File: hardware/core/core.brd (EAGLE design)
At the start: 131.8 x 142.2 mm, 280 parts, among them IC1 MAX481CSA, IC10 MAX481CSA, IC11 MAX481CSA, IC12 MAX481CSA, IC13 MAX481CSA, IC14 MAX481CSA, IC15 MAX481CSA, IC16 MAX481CSA, IC17 MAX481CSA, IC18 MAX481CSA, IC19 MAX481CSA, IC2 LD117AS12TR, IC20 MAX481CSA, IC21 MAX481CSA, IC3 MAX481CSA, IC4 MAX481CSA, IC5 MAX481CSA, IC6 MAX481CSA, IC7 MAX481CSA, IC8 MAX481CSA, IC9 MAX481CSA

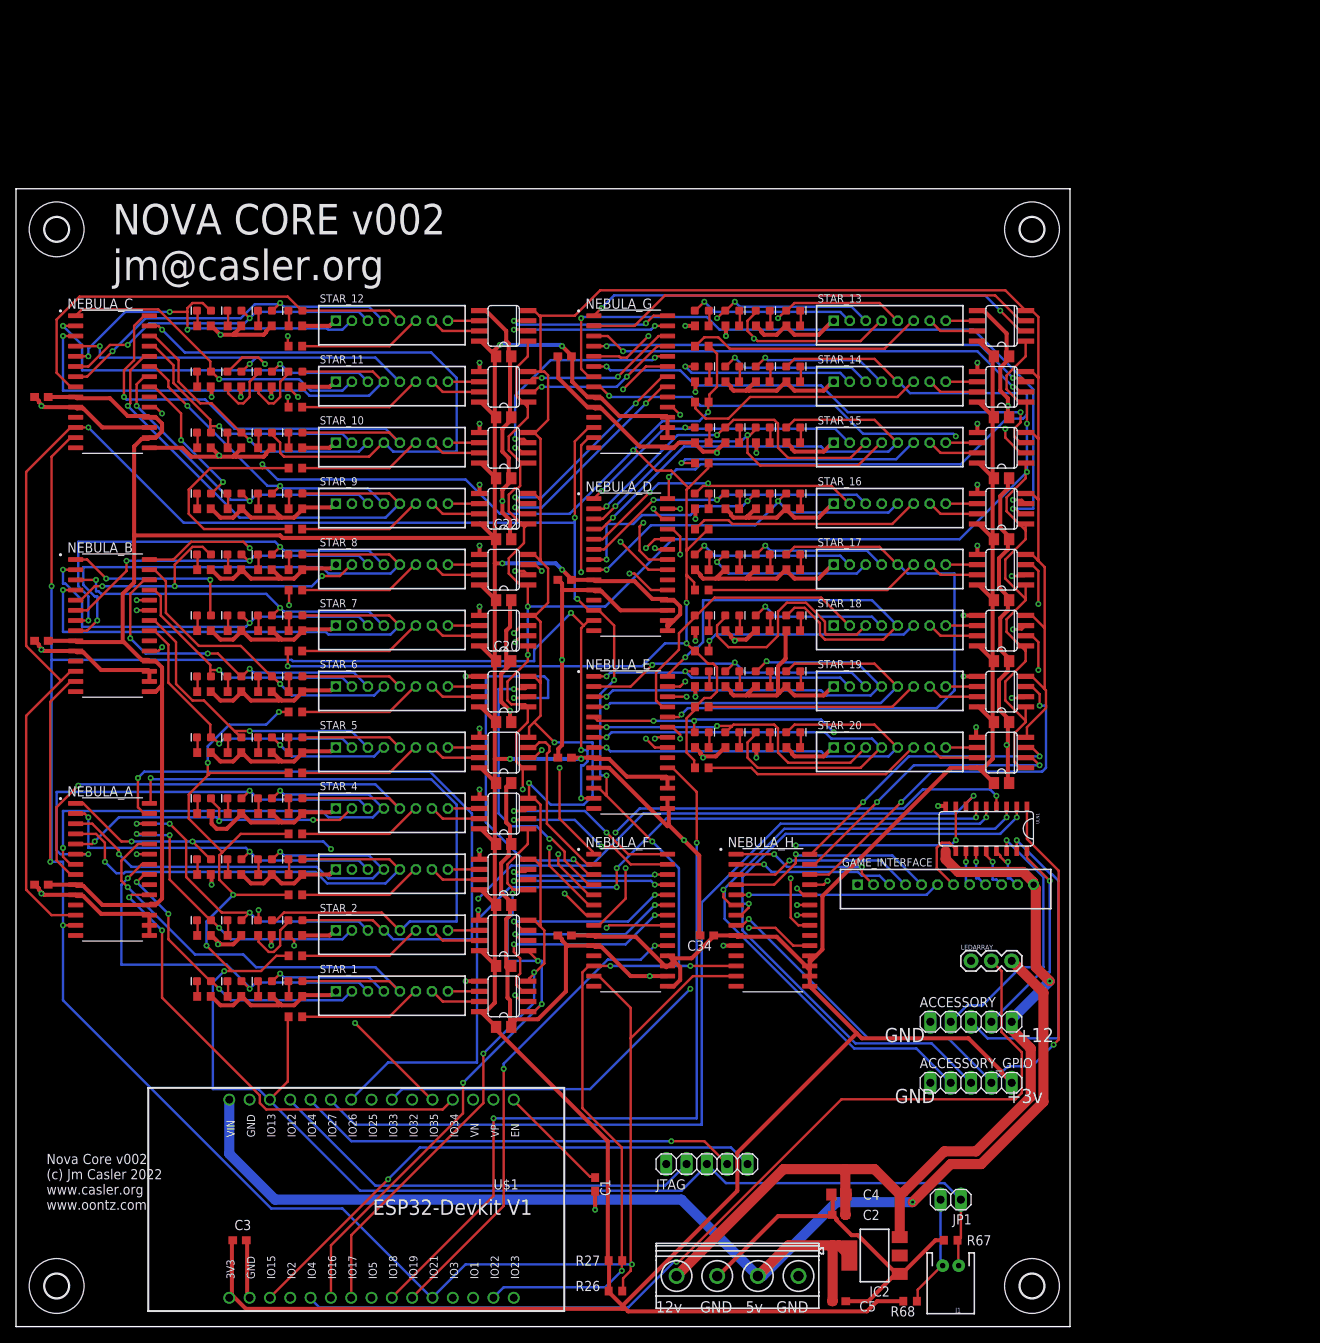
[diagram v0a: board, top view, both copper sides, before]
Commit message: Nova 3.0 in progress. Needs line drivers.
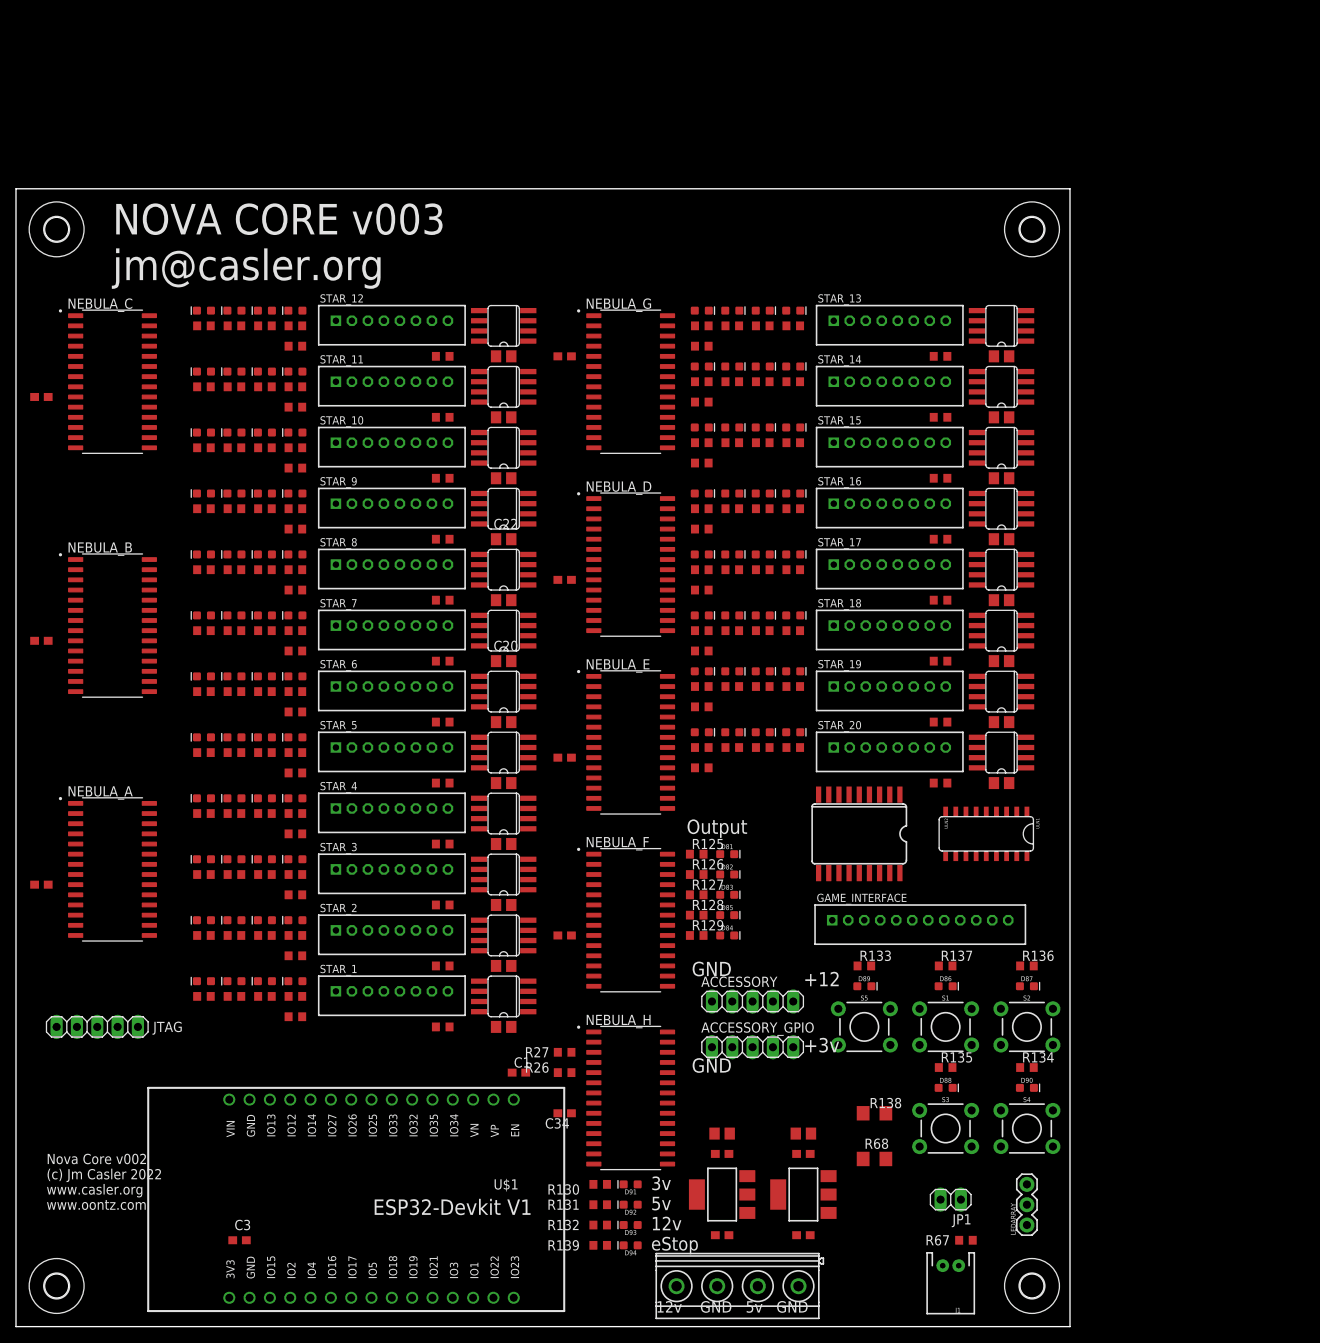
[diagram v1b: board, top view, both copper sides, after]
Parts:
- added C35, C36: 10uf, rcl:C0603
- added C6: 1uf, rcl:C0805
- added D81, D86, D91: red, SparkFun-LED:LED-0603
- added D82, D87, D92: green, SparkFun-LED:LED-0603
- added D83, D88, D93: blue, SparkFun-LED:LED-0603
- added D84, D89: white, SparkFun-LED:LED-0603
- added D85, D90, D94: yellow, SparkFun-LED:LED-0603
- added IC22: LD117AS12TR, v-reg:SOT223
- added R1, R107, R108, R109, R110, R111, R112, R113, R114, R115, R116, R117, R118, R119, R120, R121, R122, R123, R124, R2: 120, rcl:R0603
- added R125, R126, R127, R128, R129, R130, R139: 1k, rcl:R0603
- added R131: 2.2k, rcl:R0603
- added R132: 12k, rcl:R0603
- added R133, R134, R135, R136, R137: 10k, rcl:R0603
- added R138: 10, rcl:R1206
- added S1, S2, S3, S4, S5: MOMENTARY-SWITCH-SPST-PTH-6.0MM, SparkFun-Switches:TACTILE_SWITCH_PTH_6.0MM
- added ULN2: (no value), SparkFun-IC-Special-Function:SO18L
- R68: value 68 -> 10; device rcl:R0603 -> rcl:R1206
- moved JTAG 78.1 mm to (10.2, 37.5)
- moved LEDARRAY 33.8 mm to (126.4, 12.7), turned to 90 degrees
- moved C34 28.5 mm to (68.6, 26.7)
- moved NEBULA_H 28.5 mm to (76.8, 28.6)
- moved R26 28.0 mm to (68.6, 31.8)
- moved ACCESSORY_GPIO 27.7 mm to (92.1, 34.9)
- moved ACCESSORY 27.4 mm to (92.1, 40.6)
- moved R27 26.8 mm to (68.6, 34.3)
- moved IC2 20.5 mm to (88.3, 16.5)
- moved R68 18.3 mm to (107.3, 21.0), turned to 0 degrees
- moved C1 16.9 mm to (62.9, 31.8), turned to 0 degrees
- moved C5 16.8 mm to (88.3, 11.4)
- moved C2 16.5 mm to (88.3, 21.6)
- moved C4 16.5 mm to (88.3, 24.1)
- moved GAME_INTERFACE 5.46 mm to (113.0, 50.8)
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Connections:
- new net N$151: D84.A, R129.2
- new net N$152: D85.A, R128.2
- new net N$153: D83.A, R127.2
- new net N$154: D82.A, R126.2
- new net N$155: D81.A, R125.2
- new net N$156: D91.C, R130.1
- new net N$157: D92.C, R131.1
- new net N$158: D93.C, R132.1
- new net N$159: D94.C, R139.1
- net +12V: now also D93.A, ULN2.10
- net +3V3: now also C36.1, D86.A, D87.A, D88.A, D89.A, D90.A, D91.A, IC22.4, R133.1, R134.1, R135.1, R136.1, R137.1, R138.2
- net +5V: now also C35.1, C6.1, D92.A, IC22.3, R125.1, R126.1, R127.1, R128.1, R129.1
- net 13: now also D94.A
- net 23: now also ULN2.8
- net 25: now also ULN2.7
- net 26: now also ULN2.6
- net 27: now also ULN2.5
- net 32: now also ULN2.4
- net GND: now also C35.2, C36.2, C6.2, IC22.1, R130.2, R131.2, R132.2, R139.2, S1.3, S2.3, S3.3, S4.3, S5.3, ULN2.9
- net H10: now also D88.C, R135.2, S3.1
- net H11: now also D90.C, R134.2, S4.1
- net H12: now also D89.C, R133.2, S5.1
- net H13: now also ULN2.3
- net H14: now also ULN2.2
- net H15: now also ULN2.1
- net H8: now also D86.C, R137.2, S1.1
- net H9: now also D87.C, R136.2, S2.1
- net N$108: now also R1.2
- net N$109: now also R1.1
- net N$110: now also R2.2
- net N$111: now also R2.1
- net N$112: now also R107.2
- net N$113: now also R107.1
- net N$114: now also R108.2
- net N$115: now also R108.1
- net N$116: now also R109.2
- net N$117: now also R109.1
- net N$118: now also R110.2
- net N$119: now also R110.1
- net N$120: now also R111.2
- net N$121: now also R111.1
- net N$122: now also R112.2
- net N$123: now also R112.1
- net N$124: now also R113.2
- net N$125: now also R113.1
- net N$126: now also R114.2
- net N$127: now also R114.1
- net N$128: now also R115.2
- net N$129: now also R115.1
- net N$130: now also R116.2
- net N$131: now also R116.1
- net N$132: now also R117.2
- net N$133: now also R117.1
- net N$134: now also R118.2
- net N$135: now also R118.1
- net N$136: now also R119.2
- net N$137: now also R119.1
- net N$138: now also R120.2
- net N$139: now also R120.1
- net N$140: now also R121.2
- net N$141: now also R121.1
- net N$142: now also R122.2
- net N$143: now also R122.1
- net N$144: now also R123.2
- net N$145: now also R123.1
- net N$146: now also R124.2
- net N$147: now also R124.1
- net N$148: now also ULN2.16
- net N$149: now also ULN2.17
- net N$150: now also ULN2.18
- net N$51: now also D81.C, ULN2.11
- net N$56: now also D82.C, ULN2.12
- net N$57: now also D83.C, ULN2.13
- net N$58: now also D85.C, ULN2.14
- net N$59: now also D84.C, ULN2.15
- net N$89: now also R138.1
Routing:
- net GND: track 750.6 -> 0.00 mm, vias 50 -> 0
- net +3V3: track 726.2 -> 0.00 mm, vias 6 -> 0
- net 13: track 470.0 -> 0.00 mm, vias 14 -> 0
- net 21/SDA: track 366.5 -> 0.00 mm, vias 8 -> 0
- net 16: track 309.2 -> 0.00 mm, vias 9 -> 0
- net 17: track 305.9 -> 0.00 mm, vias 4 -> 0
- net 22/SCL: track 296.7 -> 0.00 mm, vias 9 -> 0
- net +5V: track 163.7 -> 0.00 mm, vias 1 -> 0
- net 33: track 137.3 -> 0.00 mm, vias 3 -> 0
- net 36: track 120.4 -> 0.00 mm, vias 1 -> 0
- net 4: track 118.7 -> 0.00 mm, vias 1 -> 0
- net 27: track 116.8 -> 0.00 mm, vias 1 -> 0
- net +12V: track 111.2 -> 0.00 mm, vias 1 -> 0
- net 26: track 105.9 -> 0.00 mm, vias 3 -> 0
- net 25: track 99.6 -> 0.00 mm, vias 2 -> 0
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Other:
- board text added: "3v 5v 12v eStop"
- board text added: "NOVA CORE v003 jm@casler.org"
- board text added: "Output"
- board text removed: "NOVA CORE v002 jm@casler.org"

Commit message: start of adding ULN to the outputs
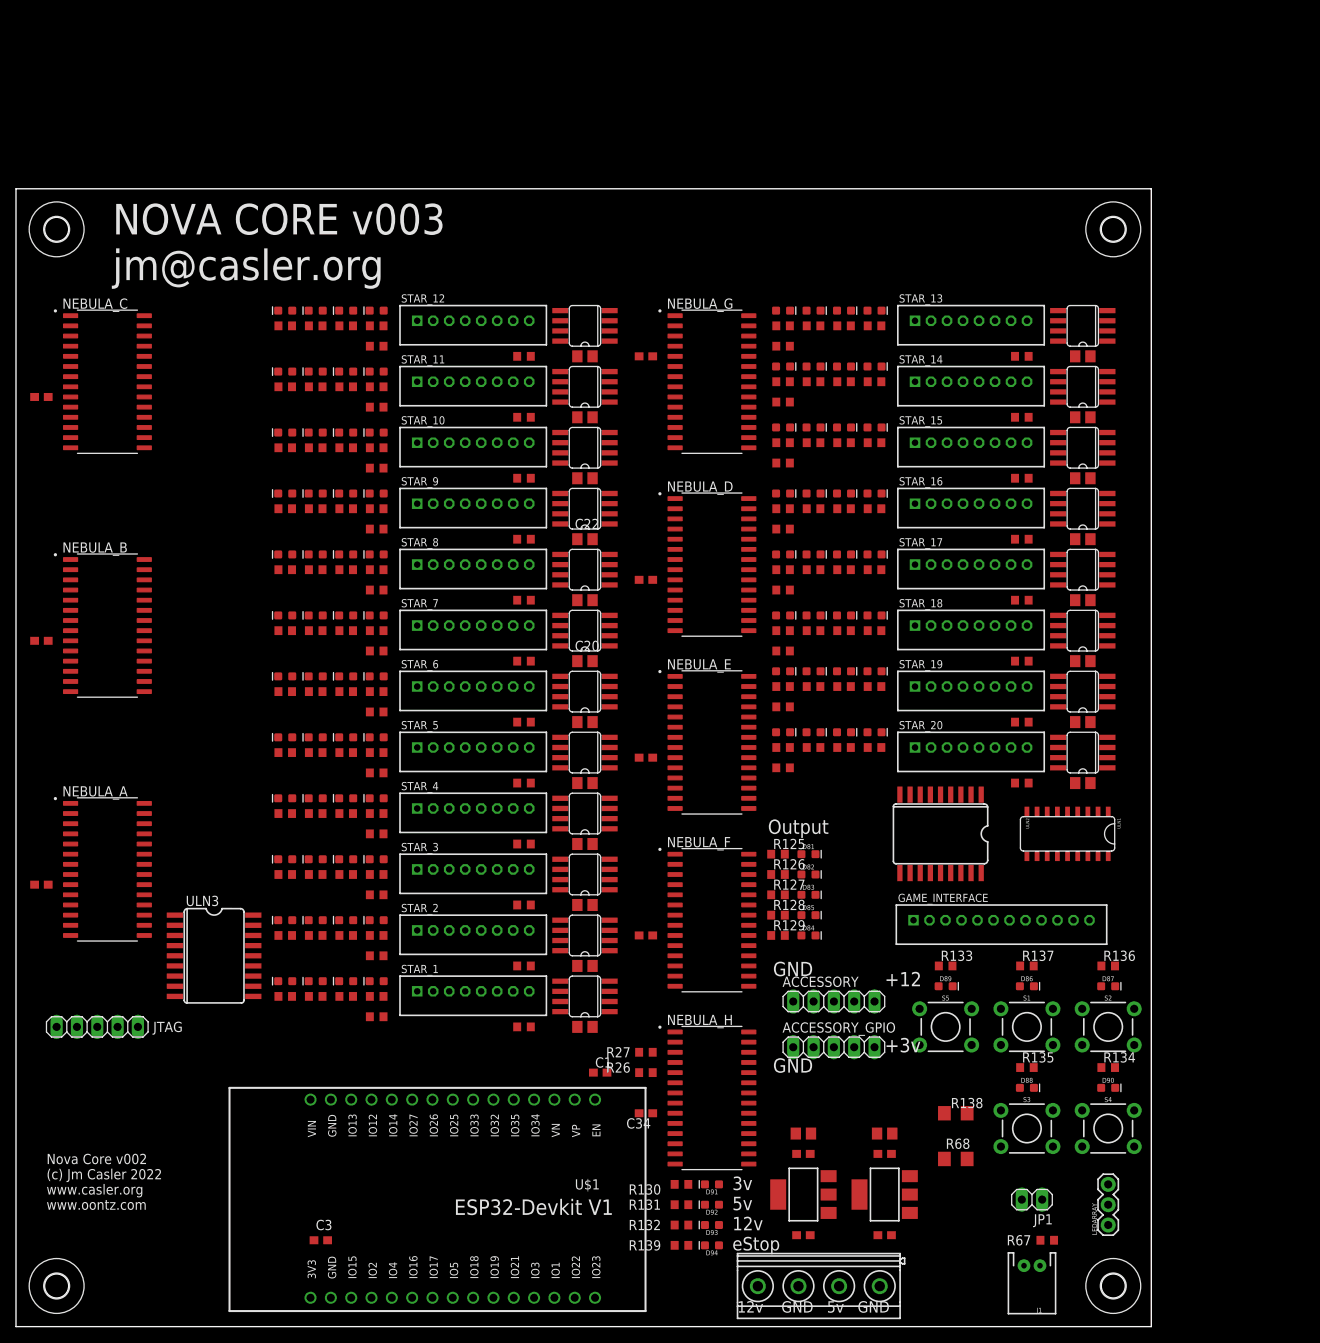
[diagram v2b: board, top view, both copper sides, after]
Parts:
- added ULN3: (no value), SparkFun-IC-Special-Function:SO18L
- moved D1 10.2 mm to (95.9, 127.0)
- moved D53 10.2 mm to (95.9, 120.0)
- moved D57 10.2 mm to (95.9, 112.4)
- moved D61 10.2 mm to (95.9, 104.1)
- moved D65 10.2 mm to (95.9, 96.5)
- moved D69 10.2 mm to (95.9, 88.9)
- moved D73 10.2 mm to (95.9, 81.9)
- moved D77 10.2 mm to (95.9, 74.3)
- moved D87 10.2 mm to (136.5, 42.5)
- moved D90 10.2 mm to (136.5, 29.8)
- moved D91 10.2 mm to (87.0, 17.8)
- moved D92 10.2 mm to (87.0, 15.2)
- moved D93 10.2 mm to (87.0, 12.7)
- moved D94 10.2 mm to (87.0, 10.2)
- moved LEDARRAY 10.2 mm to (136.5, 12.7)
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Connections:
- new net N$160: R3.1, STAR_1.2, ULN3.11
- new net N$161: R4.1, STAR_1.3, ULN3.12
- new net N$162: R5.1, STAR_1.4, ULN3.13
- new net N$163: R6.1, STAR_1.5, ULN3.14
- new net N$164: R10.1, STAR_2.5, ULN3.18
- new net N$165: R9.1, STAR_2.4, ULN3.17
- new net N$166: R8.1, STAR_2.3, ULN3.16
- new net N$167: R7.1, STAR_2.2, ULN3.15
- net +12V: now also ULN3.10
- net +5V: now also D2.A, D3.A, D4.A, D5.A, D6.A, D7.A, D8.A, D9.A
- net A0: now also ULN3.8; no longer D2.A, STAR_1.2
- net A1: now also ULN3.7; no longer D3.A, STAR_1.3
- net A2: now also ULN3.6; no longer D4.A, STAR_1.4
- net A3: now also ULN3.5; no longer D5.A, STAR_1.5
- net A4: now also ULN3.4; no longer D6.A, STAR_2.2
- net A5: now also ULN3.3; no longer D7.A, STAR_2.3
- net A6: now also ULN3.2; no longer D8.A, STAR_2.4
- net A7: now also ULN3.1; no longer D9.A, STAR_2.5
- net GND: now also ULN3.9; no longer R10.1, R3.1, R4.1, R5.1, R6.1, R7.1, R8.1, R9.1
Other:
- board size 131.8 x 142.2 mm -> 141.9 x 142.2 mm
